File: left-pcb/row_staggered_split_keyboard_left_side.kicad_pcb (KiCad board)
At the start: 2 copper layers, 146 x 132 mm, 151 parts, among them J1 Conn_01x02, SW1 SW_SPST, SW10 SW_SPST, SW11 SW_SPST, SW12 SW_SPST, SW13 SW_SPST, SW14 SW_SPST, SW15 SW_SPST, SW16 SW_SPST, SW17 SW_SPST, SW18 SW_SPST, SW19 SW_SPST, SW2 SW_SPST, SW20 SW_SPST, SW21 SW_SPST, SW22 SW_SPST, SW23 SW_SPST, SW24 SW_SPST, SW25 SW_SPST, SW26 SW_SPST, SW27 SW_SPST, SW28 SW_SPST, SW29 SW_SPST, SW3 SW_SPST, SW30 SW_SPST, SW31 SW_SPST, SW32 SW_SPST, SW33 SW_SPST, SW34 SW_SPST, SW35 SW_SPST, SW4 SW_SPST, SW5 SW_SPST, SW6 SW_SPST, SW7 SW_SPST, SW8 SW_SPST, SW9 SW_SPST, U1 SN74LVC1T45DBV

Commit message: Adding values to Diodes and adding stabilizers to 2U switches
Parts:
- added H5: Stabilizer_Cherry_MX_2.00u, PCM_Mounting_Keyboard_Stabilizer:Stabilizer_Cherry_MX_2.00u, F.Cu at (51.0, 135.5)
- added H6: Stabilizer_Cherry_MX_2.00u, PCM_Mounting_Keyboard_Stabilizer:Stabilizer_Cherry_MX_2.00u, F.Cu at (124.9, 154.6)
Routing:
- net /ROW1: track 195.5 -> 185.4 mm, vias 10 -> 5
- net GND: track 165.6 -> 158.7 mm, vias 79 -> 76
- net /COL5: track 155.6 -> 161.2 mm
- net Net-(D9-A): track 8.70 -> 4.35 mm
- net Net-(D7-A): track 8.70 -> 4.35 mm
- net Net-(D5-A): track 8.70 -> 4.35 mm
- net Net-(D3-A): track 8.70 -> 4.35 mm
- net Net-(D1-A): track 8.70 -> 4.35 mm
- net +3V3: track 2.00 -> 5.30 mm
- net /R5C6/DOUT: track 119.2 -> 122.2 mm
- net /R4C6/DOUT: track 107.6 -> 105.1 mm
- net +5V: track 2.00 -> 4.40 mm
- net /COL6: track 105.2 -> 107.1 mm
- net /COL1: track 241.7 -> 239.8 mm
- net /ROW6: track 228.9 -> 230.8 mm
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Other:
- board text added: "BKTICK"
- board text added: "CAPS LK"
- board text removed: "BACKTICK"
- board text removed: "CAPS LOCK"

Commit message: forgot to update diode values in PCB
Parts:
- D1, D11, D13, D15, D17, D19, D21, D23, D25, D27, D29, D3, D31, D33, D35, D37, D39, D41, D43, D45, D47, D49, D5, D51, D53, D55, D57, D59, D61, D63, D65, D67, D69, D7, D9: value D_Small -> 1N4148W
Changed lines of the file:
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@@
 			)
 		)
-		(property "Value" "D_Small"
+		(property "Value" "1N4148W"
 			(at 0 -2.1 90)
 			(layer "B.Fab")
@@
 			)
 		)
-		(property "Value" "D_Small"
+		(property "Value" "1N4148W"
 			(at 0 -2.1 90)
 			(layer "B.Fab")
@@
 			)
 		)
-		(property "Value" "D_Small"
+		(property "Value" "1N4148W"
 			(at 0 -2.1 90)
 			(layer "B.Fab")
@@
 			)
 		)
-		(property "Value" "D_Small"
+		(property "Value" "1N4148W"
 			(at 0 -2.1 90)
 			(layer "B.Fab")
@@
 			)
 		)
-		(property "Value" "D_Small"
+		(property "Value" "1N4148W"
 			(at 0 -2.1 90)
 			(layer "B.Fab")
@@
 			)
 		)
-		(property "Value" "D_Small"
+		(property "Value" "1N4148W"
 			(at 0 -2.1 90)
 			(layer "B.Fab")
@@
 			)
 		)
-		(property "Value" "D_Small"
+		(property "Value" "1N4148W"
 			(at 0 -2.1 90)
 			(layer "B.Fab")
@@
 			)
 		)
-		(property "Value" "D_Small"
+		(property "Value" "1N4148W"
 			(at 0 -2.1 90)
 			(layer "B.Fab")
@@
 			)
 		)
-		(property "Value" "D_Small"
+		(property "Value" "1N4148W"
 			(at 0 -2.1 90)
 			(layer "B.Fab")
@@
 			)
 		)
-		(property "Value" "D_Small"
+		(property "Value" "1N4148W"
 			(at 0 -2.1 90)
 			(layer "B.Fab")
@@
 			)
 		)
-		(property "Value" "D_Small"
+		(property "Value" "1N4148W"
 			(at 0 -2.1 90)
 			(layer "B.Fab")
@@
 			)
 		)
-		(property "Value" "D_Small"
+		(property "Value" "1N4148W"
 			(at 0 -2.1 90)
 			(layer "B.Fab")
@@
 			)
 		)
-		(property "Value" "D_Small"
+		(property "Value" "1N4148W"
 			(at 0 -2.1 90)
 			(layer "B.Fab")
@@
 			)
 		)
-		(property "Value" "D_Small"
+		(property "Value" "1N4148W"
 			(at 0 -2.1 90)
 			(layer "B.Fab")
@@
 			)
 		)
-		(property "Value" "D_Small"
+		(property "Value" "1N4148W"
 			(at 0 -2.1 90)
 			(layer "B.Fab")
@@
 			)
 		)
-		(property "Value" "D_Small"
+		(property "Value" "1N4148W"
 			(at 0 -2.1 90)
 			(layer "B.Fab")
@@
 			)
 		)
-		(property "Value" "D_Small"
+		(property "Value" "1N4148W"
 			(at 0 -2.1 90)
 			(layer "B.Fab")
@@
 			)
 		)
-		(property "Value" "D_Small"
+		(property "Value" "1N4148W"
 			(at 0 -2.1 90)
 			(layer "B.Fab")
@@
 			)
 		)
-		(property "Value" "D_Small"
+		(property "Value" "1N4148W"
 			(at 0 -2.1 90)
 			(layer "B.Fab")
@@
 			)
 		)
-		(property "Value" "D_Small"
+		(property "Value" "1N4148W"
 			(at 0 -2.1 90)
 			(layer "B.Fab")
@@
 			)
 		)
-		(property "Value" "D_Small"
+		(property "Value" "1N4148W"
 			(at 0 -2.1 90)
 			(layer "B.Fab")
@@
 			)
 		)
-		(property "Value" "D_Small"
+		(property "Value" "1N4148W"
 			(at 0 -2.1 90)
 			(layer "B.Fab")
@@
 			)
 		)
-		(property "Value" "D_Small"
+		(property "Value" "1N4148W"
 			(at 0 -2.1 90)
 			(layer "B.Fab")
@@
 			)
 		)
-		(property "Value" "D_Small"
+		(property "Value" "1N4148W"
 			(at 0 -2.1 90)
 			(layer "B.Fab")
@@
 			)
 		)
-		(property "Value" "D_Small"
+		(property "Value" "1N4148W"
 			(at 0 -2.1 90)
 			(layer "B.Fab")
@@
 			)
 		)
-		(property "Value" "D_Small"
+		(property "Value" "1N4148W"
 			(at 0 -2.1 90)
 			(layer "B.Fab")
@@
 			)
 		)
-		(property "Value" "D_Small"
+		(property "Value" "1N4148W"
 			(at 0 -2.1 90)
 			(layer "B.Fab")
@@
 			)
 		)
-		(property "Value" "D_Small"
+		(property "Value" "1N4148W"
 			(at 0 -2.1 90)
 			(layer "B.Fab")
@@
 			)
 		)
-		(property "Value" "D_Small"
+		(property "Value" "1N4148W"
 			(at 0 -2.1 90)
 			(layer "B.Fab")
@@
 			)
 		)
-		(property "Value" "D_Small"
+		(property "Value" "1N4148W"
 			(at 0 -2.1 90)
 			(layer "B.Fab")
@@
 			)
 		)
-		(property "Value" "D_Small"
+		(property "Value" "1N4148W"
 			(at 0 -2.1 90)
 			(layer "B.Fab")
@@
 			)
 		)
-		(property "Value" "D_Small"
+		(property "Value" "1N4148W"
 			(at 0 -2.1 90)
 			(layer "B.Fab")
@@
 			)
 		)
-		(property "Value" "D_Small"
+		(property "Value" "1N4148W"
 			(at 0 -2.1 90)
 			(layer "B.Fab")
@@
 			)
 		)
-		(property "Value" "D_Small"
+		(property "Value" "1N4148W"
 			(at 0 -2.1 90)
 			(layer "B.Fab")
@@
 			)
 		)
-		(property "Value" "D_Small"
+		(property "Value" "1N4148W"
 			(at 0 -2.1 90)
 			(layer "B.Fab")

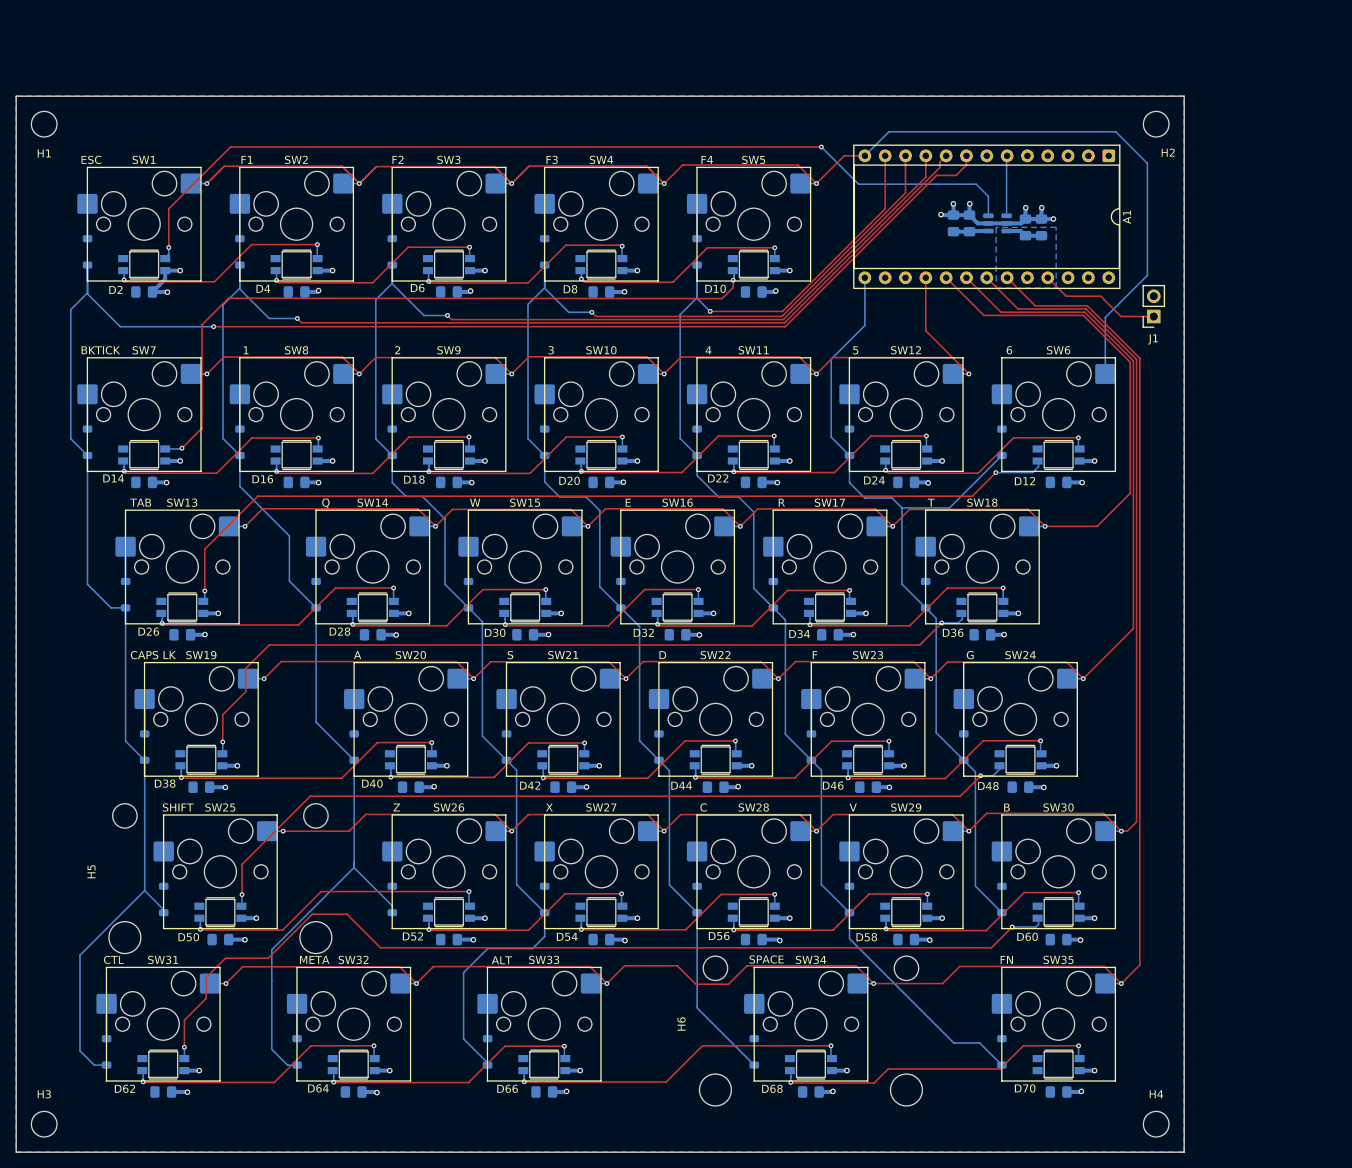
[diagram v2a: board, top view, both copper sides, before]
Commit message: Added extra column to left hand keyboard
Matching size to right hand side.
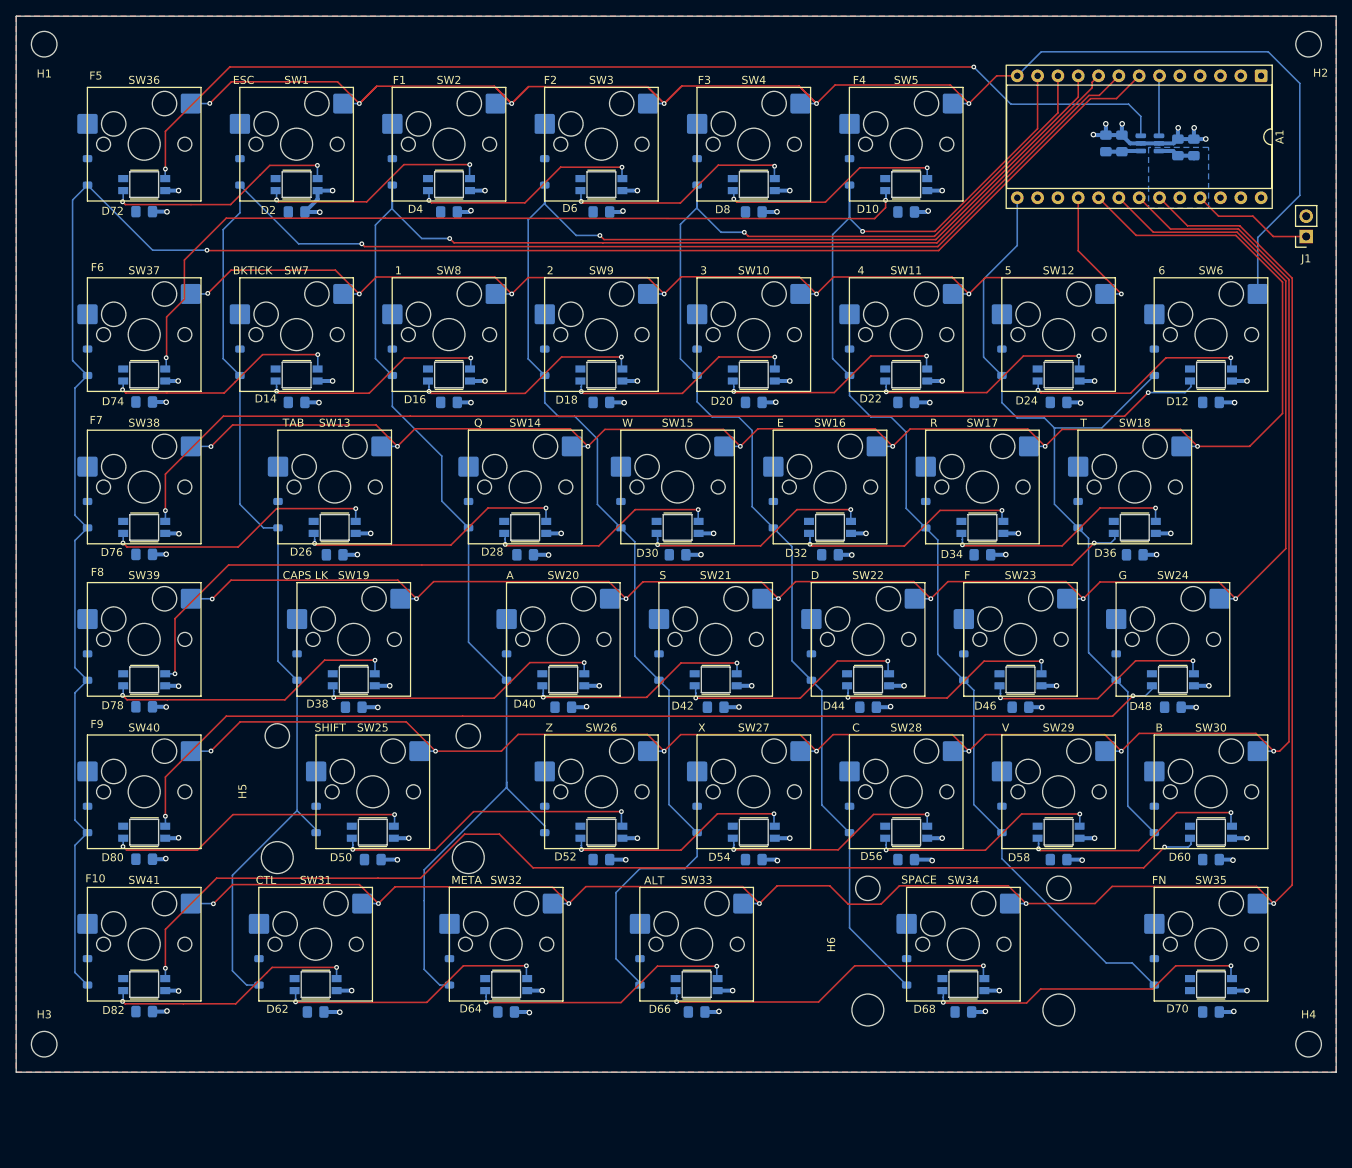
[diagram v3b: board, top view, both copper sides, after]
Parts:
- added C40: 100nF, Capacitor_SMD:C_0805_2012Metric_Pad1.18x1.45mm_HandSolder, B.Cu at (41.5, 53.0)
- added C41: 100nF, Capacitor_SMD:C_0805_2012Metric_Pad1.18x1.45mm_HandSolder, B.Cu at (41.5, 76.8)
- added C42: 100nF, Capacitor_SMD:C_0805_2012Metric_Pad1.18x1.45mm_HandSolder, B.Cu at (41.5, 95.8)
- added C43: 100nF, Capacitor_SMD:C_0805_2012Metric_Pad1.18x1.45mm_HandSolder, B.Cu at (41.5, 114.9)
- added C44: 100nF, Capacitor_SMD:C_0805_2012Metric_Pad1.18x1.45mm_HandSolder, B.Cu at (41.5, 133.9)
- added C45: 100nF, Capacitor_SMD:C_0805_2012Metric_Pad1.18x1.45mm_HandSolder, B.Cu at (41.5, 153.0)
- added D71: 1N4148W, Diode_SMD:D_SOD-123, B.Cu at (34.4, 48.0)
- added D72: SK6812MINI-E, SW-Adafruit:LED_SK6812MINI-E_REVERSE_MOUNT_3.2x2.8mm_P1.09mm, F.Cu at (41.5, 49.6)
- added D73: 1N4148W, Diode_SMD:D_SOD-123, B.Cu at (34.4, 71.8)
- added D74: SK6812MINI-E, SW-Adafruit:LED_SK6812MINI-E_REVERSE_MOUNT_3.2x2.8mm_P1.09mm, F.Cu at (41.5, 73.4)
- added D75: 1N4148W, Diode_SMD:D_SOD-123, B.Cu at (34.4, 90.9)
- added D76: SK6812MINI-E, SW-Adafruit:LED_SK6812MINI-E_REVERSE_MOUNT_3.2x2.8mm_P1.09mm, F.Cu at (41.5, 92.5)
- added D77: 1N4148W, Diode_SMD:D_SOD-123, B.Cu at (34.4, 109.9)
- added D78: SK6812MINI-E, SW-Adafruit:LED_SK6812MINI-E_REVERSE_MOUNT_3.2x2.8mm_P1.09mm, F.Cu at (41.5, 111.5)
- added D79: 1N4148W, Diode_SMD:D_SOD-123, B.Cu at (34.4, 129.0)
- added D80: SK6812MINI-E, SW-Adafruit:LED_SK6812MINI-E_REVERSE_MOUNT_3.2x2.8mm_P1.09mm, F.Cu at (41.5, 130.6)
- added D81: 1N4148W, Diode_SMD:D_SOD-123, B.Cu at (34.4, 148.0)
- added D82: SK6812MINI-E, SW-Adafruit:LED_SK6812MINI-E_REVERSE_MOUNT_3.2x2.8mm_P1.09mm, F.Cu at (41.5, 149.6)
- added SW36: SW_SPST, PCM_Switch_Keyboard_Hotswap_Kailh:SW_Hotswap_Kailh_MX_1.00u, F.Cu at (41.5, 44.6)
- added SW37: SW_SPST, PCM_Switch_Keyboard_Hotswap_Kailh:SW_Hotswap_Kailh_MX_1.00u, F.Cu at (41.5, 68.4)
- added SW38: SW_SPST, PCM_Switch_Keyboard_Hotswap_Kailh:SW_Hotswap_Kailh_MX_1.00u, F.Cu at (41.5, 87.4)
- added SW39: SW_SPST, PCM_Switch_Keyboard_Hotswap_Kailh:SW_Hotswap_Kailh_MX_1.00u, F.Cu at (41.5, 106.5)
- added SW40: SW_SPST, PCM_Switch_Keyboard_Hotswap_Kailh:SW_Hotswap_Kailh_MX_1.00u, F.Cu at (41.5, 125.5)
- added SW41: SW_SPST, PCM_Switch_Keyboard_Hotswap_Kailh:SW_Hotswap_Kailh_MX_1.00u, F.Cu at (41.5, 144.6)
- H1, H2, H3, H4: value MountingHole -> M3
- H5, H6: value Stabilizer_Cherry_MX_2.00u -> 2U Stabilizer
- moved C1 21.5 mm to (172.7, 45.0)
- moved C10 21.5 mm to (174.9, 76.8)
- moved C15 21.5 mm to (136.8, 76.8)
- moved C18 21.5 mm to (89.2, 95.9)
- moved C2 21.5 mm to (170.7, 45.0)
- moved C21 21.5 mm to (146.3, 95.9)
- moved C24 21.5 mm to (93.9, 115.0)
- moved C27 21.5 mm to (151.1, 115.0)
- moved C3 21.5 mm to (163.7, 44.5)
- moved C31 21.5 mm to (117.7, 134.0)
- moved C33 21.5 mm to (155.8, 134.0)
- moved C34 21.5 mm to (174.9, 134.0)
- moved C39 21.5 mm to (174.9, 153.1)
- moved C4 21.5 mm to (161.7, 44.5)
- moved C9 21.5 mm to (136.8, 53.0)
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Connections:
- A1 pad 7: unconnected-(A1-3-Pad7) -> /COL0
- D14 pad 4: /R1C5/DOUT -> /R2C0/DOUT
- D2 pad 4: /LED_DATA -> /R1C0/DOUT
- D26 pad 4: /R1C6/DOUT -> /R3C0/DOUT
- D38 pad 4: /R3C6/DOUT -> /R4C0/DOUT
- D50 pad 4: /R4C6/DOUT -> /R5C0/DOUT
- D62 pad 4: /R5C6/DOUT -> /R6C0/DOUT
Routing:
- net /COL0: track 0.00 -> 250.7 mm, vias 0 -> 1
- net /R5C0/DOUT: track 0.00 -> 38.5 mm, vias 0 -> 2
- net /R4C0/DOUT: track 0.00 -> 36.8 mm, vias 0 -> 2
- net /R3C0/DOUT: track 0.00 -> 34.1 mm, vias 0 -> 2
- net /ROW5: track 208.6 -> 242.2 mm, vias 6 -> 7
- net /R6C0/DOUT: track 0.00 -> 31.5 mm, vias 0 -> 2
- net /ROW4: track 190.7 -> 220.9 mm, vias 6 -> 7
- net /R1C0/DOUT: track 0.00 -> 29.6 mm, vias 0 -> 2
- net /R2C0/DOUT: track 0.00 -> 29.5 mm, vias 0 -> 2
- net /R4C6/DOUT: track 105.1 -> 134.5 mm
- net /ROW3: track 177.1 -> 205.1 mm, vias 6 -> 7
- net /R3C6/DOUT: track 104.5 -> 130.4 mm
- net /ROW6: track 230.8 -> 256.2 mm, vias 5 -> 6
- net /R1C6/DOUT: track 115.4 -> 139.3 mm
- net /ROW2: track 127.5 -> 151.0 mm, vias 6 -> 7
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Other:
- board size 146 x 132 mm -> 165 x 132 mm
- board text added: "F10"
- board text added: "F5"
- board text added: "F6"
- board text added: "F7"
- board text added: "F8"
- board text added: "F9"
- board text added: "diode: 0X, -6Y below pad 1 of switch led: 0X, -5.05Y below center hole of switch cap: 0X, -8.425 below center hole of switch"
